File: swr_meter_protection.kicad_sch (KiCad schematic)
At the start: 36 parts, among them U1 AMS1117-5.0, U4 OP07

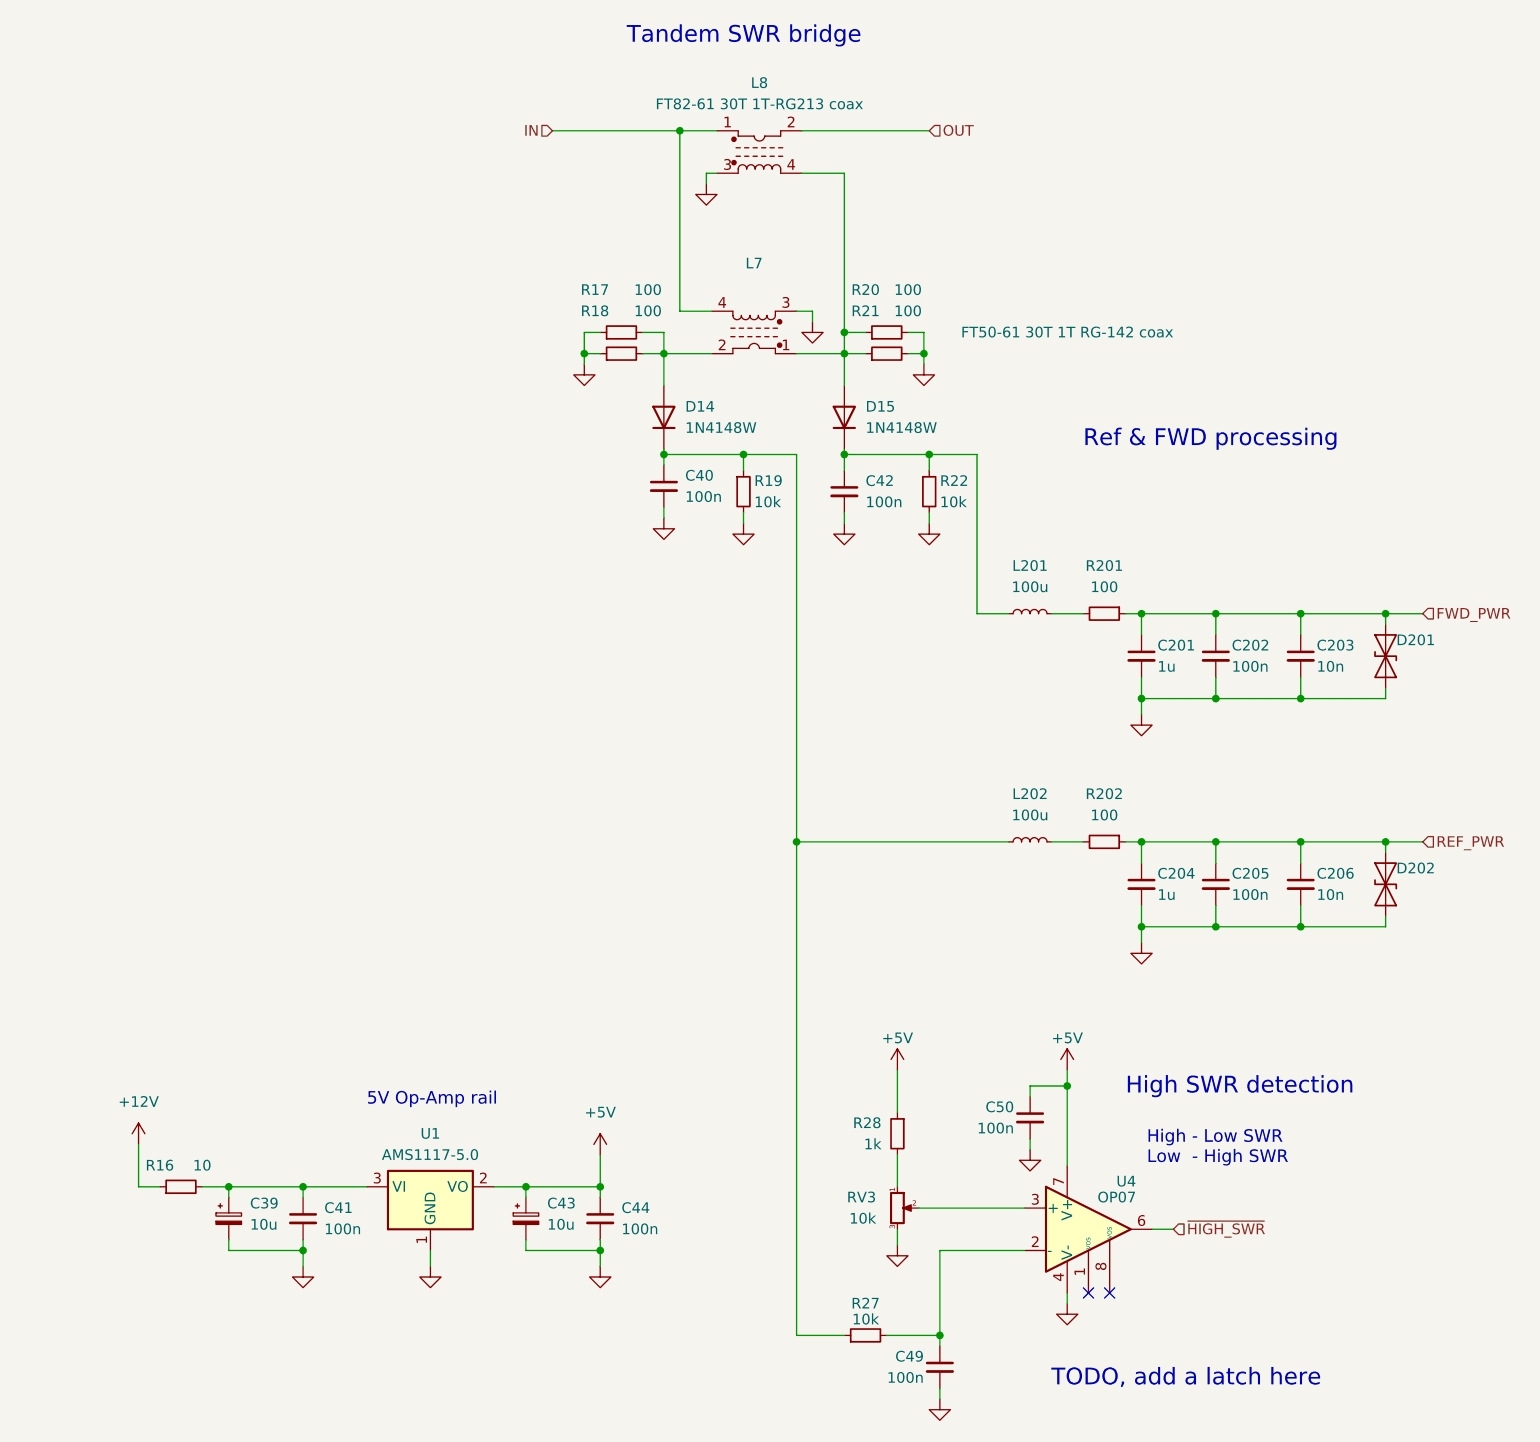
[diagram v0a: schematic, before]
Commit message: Add files via upload
Fixed DRC shorted nets error
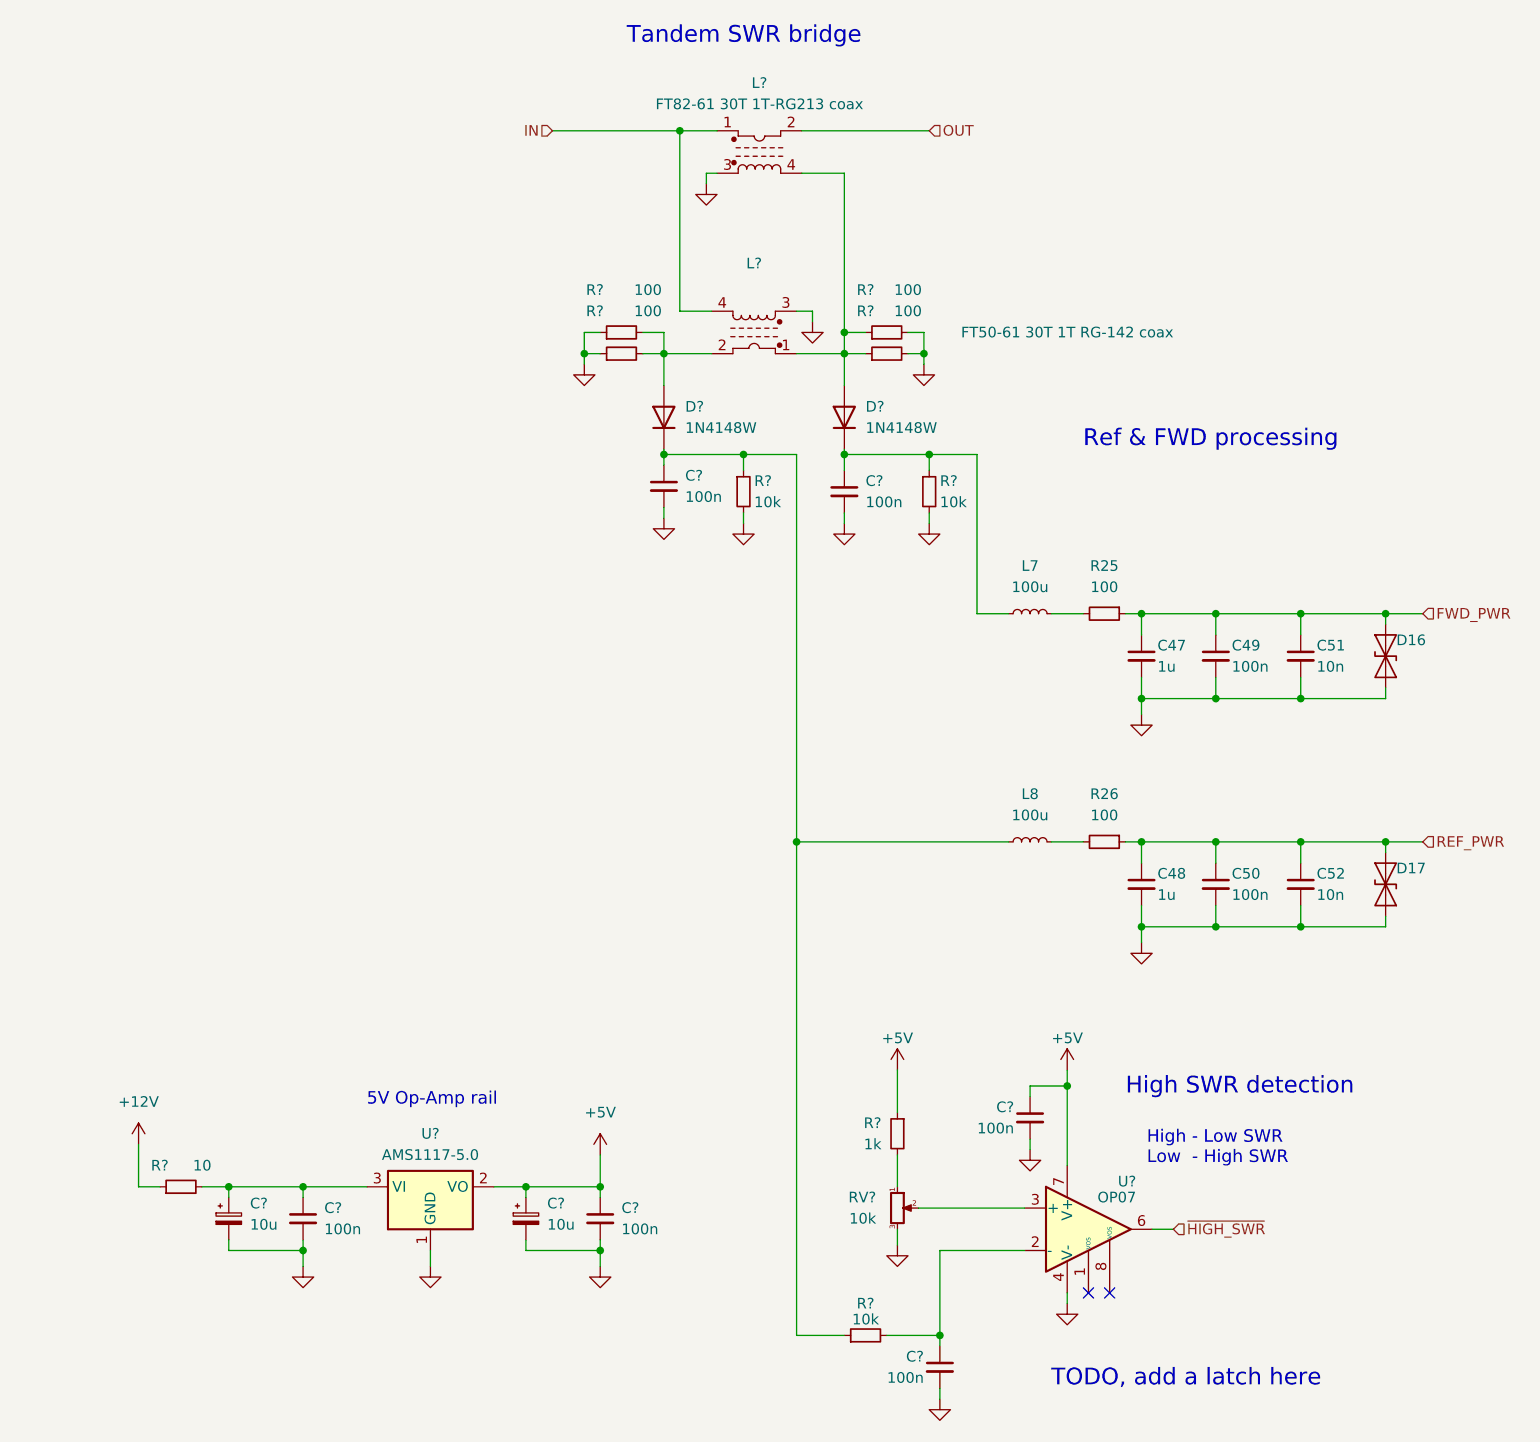
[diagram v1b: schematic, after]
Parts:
- R?: renamed from R27; footprint Resistor_SMD:R_0603_1608Metric_Pad0.98x0.95mm_HandSolder -> Resistor_SMD:R_1206_3216Metric_Pad1.30x1.75mm_HandSolder
- renumbered C201 to C47, C204 to C48, C202 to C49, C205 to C50, C203 to C51, C206 to C52, C44 to C?, C42 to C?, C50 to C?, C43 to C?, C40 to C?, C39 to C?, C41 to C?, C49 to C?, D201 to D16, D202 to D17, D15 to D?, D14 to D?, L201 to L7, L202 to L8, L8 to L?, L7 to L?, R201 to R25, R202 to R26, R21 to R?, R16 to R?, R22 to R?, R28 to R?, R19 to R?, R20 to R?, R18 to R?, R17 to R?, RV3 to RV?, U4 to U?, U1 to U?

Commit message: Used ERC on PA-Deck Schematic
Initially many hundreds of warnings, and some errors.
Apart from 8 exclusions These have all largely been fixed.
Many Symbols required updating from the appropriate library, but mostly a huge number or warnings about "symbol pin or wire end off grid connection".  Took a while, but I figured out what the problem is.
L5 & L6 exclusion referred to a TXRX library that wasn't available.
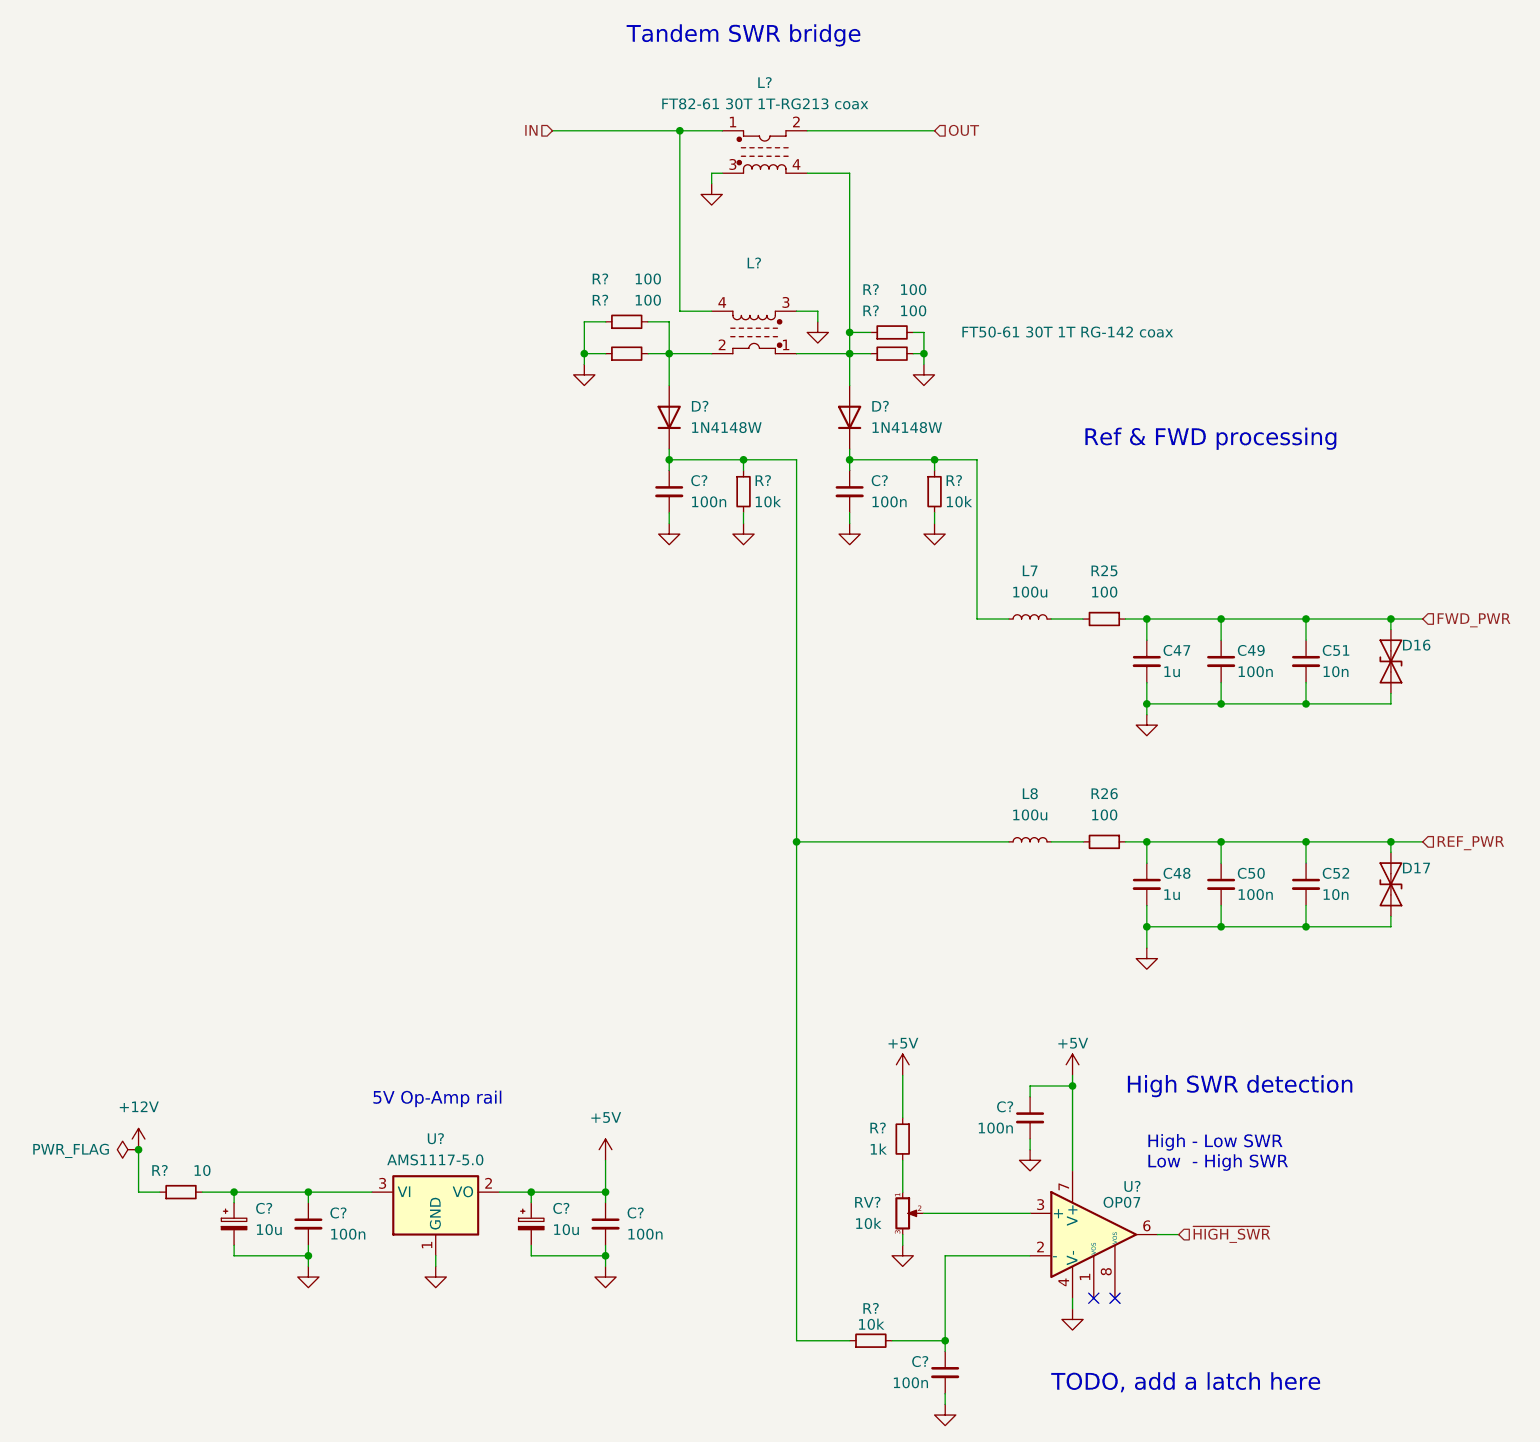
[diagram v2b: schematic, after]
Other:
- moved on the sheet: C47, C48, C49, C50, C51, C52, C?, D16, D17, D?, L7, L?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

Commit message: Ready to Order
Applied minor changes in preparation to order CPBs and components.
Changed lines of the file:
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@@
 	)
 	(junction
+		(at 50.8 162.56)
+		(diameter 0)
+		(color 0 0 0 0)
+	)
+	(junction
 		(at 83.82 170.18)
 		(diameter 0)
@@
 	(wire
 		(pts
-			(xy 48.26 162.56) (xy 55.88 162.56)
+			(xy 48.26 162.56) (xy 50.8 162.56)
 		)
 		(stroke
@@
 	(wire
 		(pts
+			(xy 50.8 162.56) (xy 55.88 162.56)
+		)
+		(stroke
+			(width 0)
+			(type default)
+		)
+	)
+	(wire
+		(pts
 			(xy 113.03 40.64) (xy 107.95 40.64)
 		)
@@
 					(unit 1)
 				)
+			)
+		)
+	)
+	(symbol
+		(lib_id "power:PWR_FLAG")
+		(at 50.8 162.56 0)
+		(unit 1)
+		(exclude_from_sim no)
+		(in_bom yes)
+		(on_board yes)
+		(dnp no)
+		(fields_autoplaced yes)
+		(property "Reference" "#FLG01"
+			(at 50.8 160.655 0)
+			(effects
+				(font
+					(size 1.27 1.27)
+				)
+				(hide yes)
+			)
+		)
+		(property "Value" "PWR_FLAG"
+			(at 50.8 157.48 0)
+			(effects
+				(font
+					(size 1.27 1.27)
+				)
+			)
+		)
+		(property "Footprint" ""
+			(at 50.8 162.56 0)
+			(effects
+				(font
+					(size 1.27 1.27)
+				)
+				(hide yes)
+			)
+		)
+		(property "Datasheet" "~"
+			(at 50.8 162.56 0)
+			(effects
+				(font
+					(size 1.27 1.27)
+				)
+				(hide yes)
+			)
+		)
+		(property "Description" "Special symbol for telling ERC where power comes from"
+			(at 50.8 162.56 0)
+			(effects
+				(font
+					(size 1.27 1.27)
+				)
+				(hide yes)
+			)
+		)
+		(pin "1"
+		)
+		(instances
+			(project "Forte_PA_Deck"
+				(path "/16ef054e-9f4a-41c5-82db-c174725d77e8/9c2873c8-c2c1-423e-860d-7050a6275c09"
+					(reference "#FLG01")
+					(unit 1)
+				)
